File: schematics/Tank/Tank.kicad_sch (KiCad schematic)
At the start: 13 parts, among them M1 LEFT MAIN, M2 RIGHT MAIN, M3 ROTATE TURRET, M4 LIFT TURRET

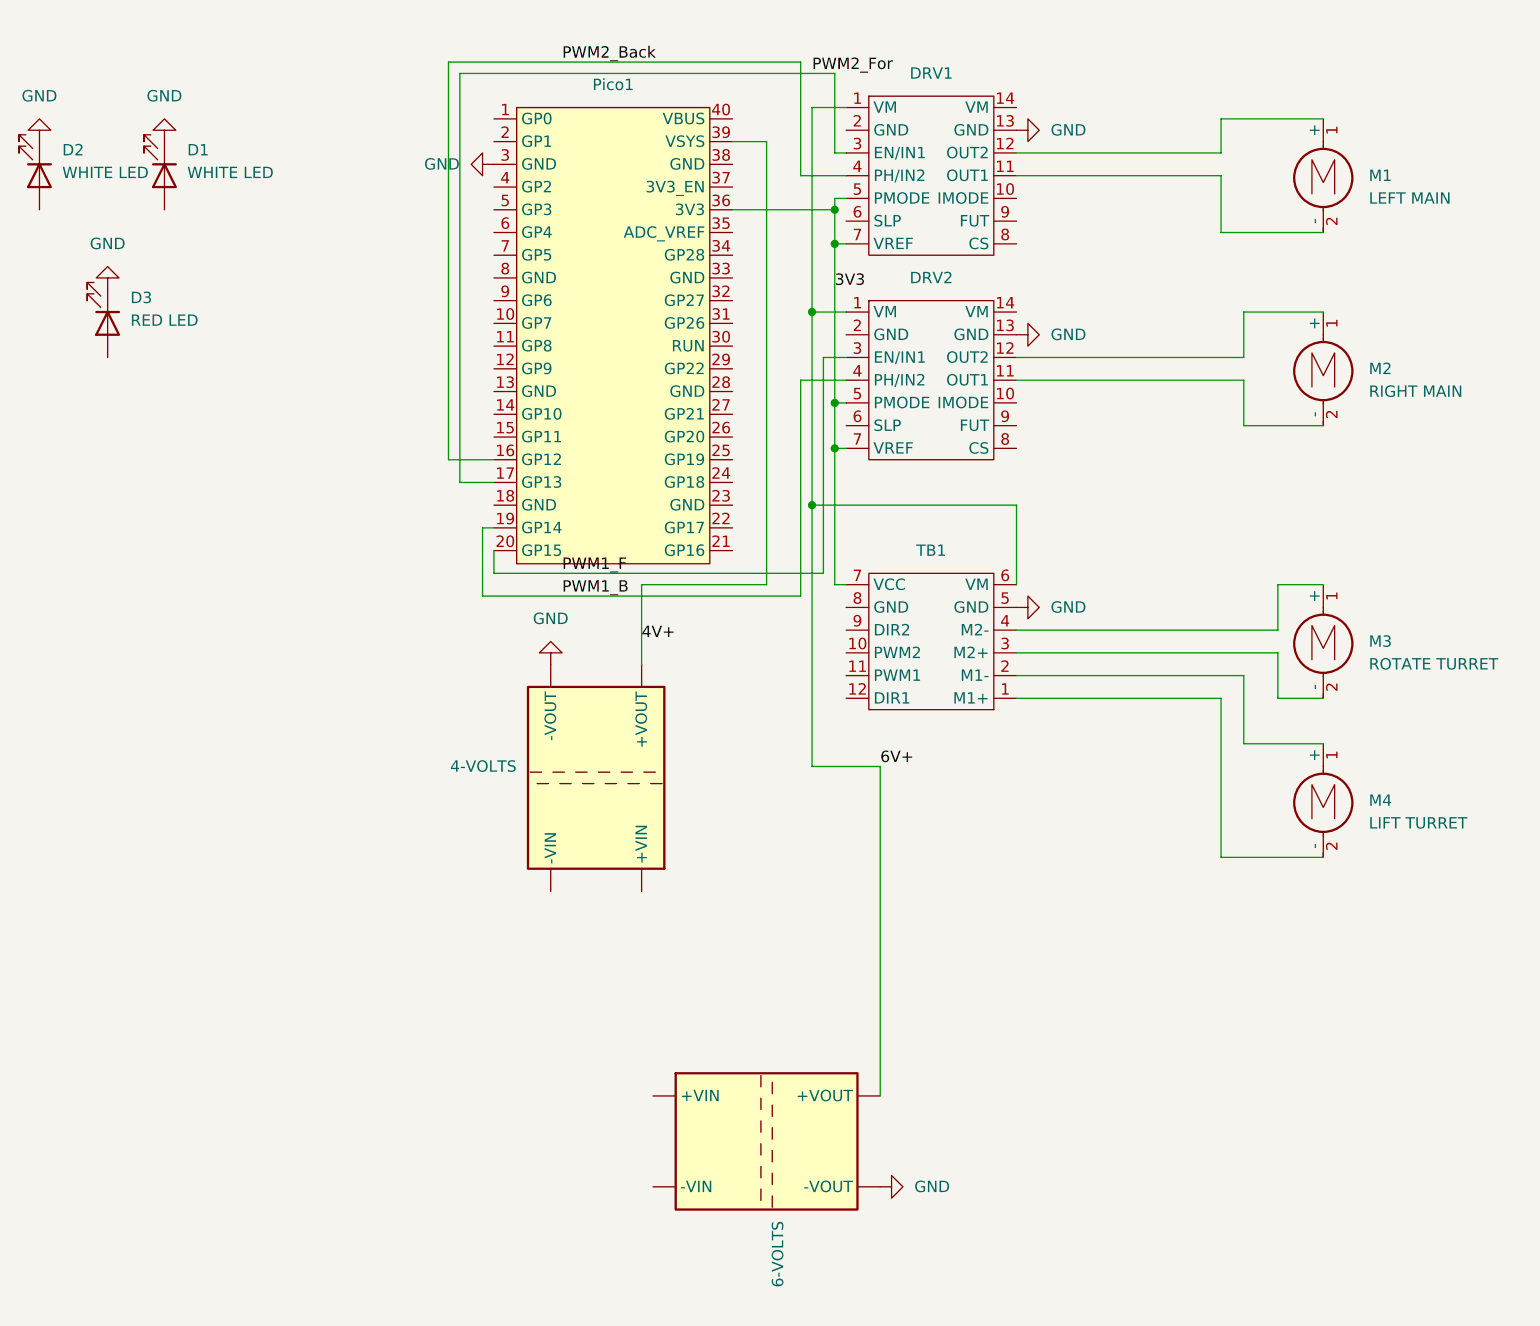
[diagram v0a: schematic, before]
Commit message: battery sampling
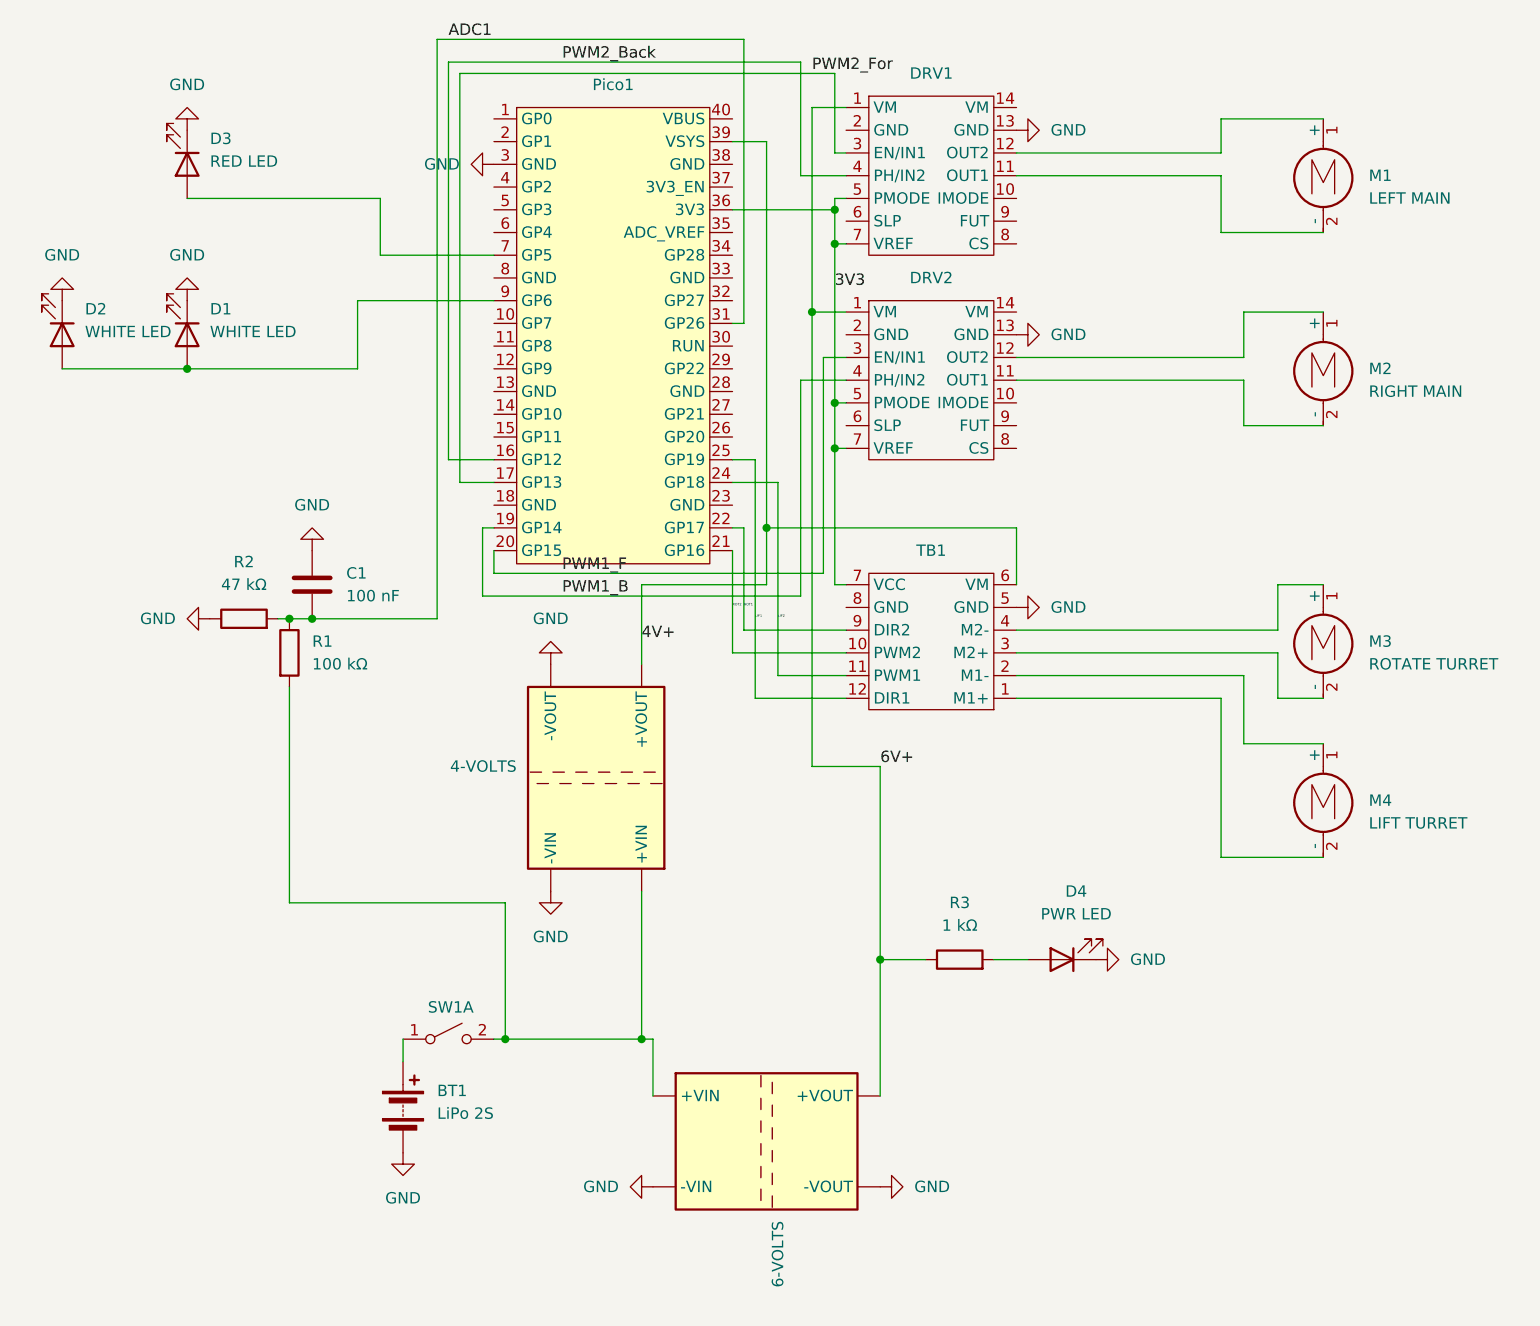
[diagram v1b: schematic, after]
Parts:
- added BT1: LiPo 2S, symbol Device:Battery
- added C1: 100 nF, symbol Device:C
- added D4: PWR LED, symbol Device:LED
- added R1: 100 kΩ, symbol Device:R
- added R2: 47 kΩ, symbol Device:R
- added R3: 1 kΩ, symbol Device:R
- added SW1: (no value), symbol Switch:SW_DPST_x2
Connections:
- net 4V+: now also TB1.6 (VM)
- net 6V+: now also R3.1; no longer TB1.6 (VM)
- net GND: now also 4-VOLTS.1 (-VIN), 6-VOLTS.1 (-VIN), BT1.2 (-), C1.1, D4.1 (K), R2.1
- net ROT2: now reaches TB1.10 (PWM2)
- net ROT2: now also Pico1.21 (GP16)
- net LIF2: now reaches TB1.11 (PWM1)
- net LIF2: now also Pico1.24 (GP18)
- net LIF1: now reaches TB1.12 (DIR1)
- net LIF1: now also Pico1.25 (GP19)
- net ROT1: now reaches TB1.9 (DIR2)
- net ROT1: now also Pico1.22 (GP17)
- net at 6-VOLTS.2 (+VIN): now also 4-VOLTS.2 (+VIN), R1.2, SW1.2 (B)
- net ADC1: now reaches Pico1.31 (GP26)
- net ADC1: now also C1.2, R1.1, R2.2
- net at Pico1.7 (GP5): now also D3.2 (A)
- net at Pico1.9 (GP6): now also D1.2 (A), D2.2 (A)
- new net: D4.2 (A), R3.2
- new net: BT1.1 (+), SW1.1 (A)
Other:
- moved on the sheet: D1, D2, D3
